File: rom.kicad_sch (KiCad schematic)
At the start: 3 parts, among them U1 74HCT1G08, U2 28C256

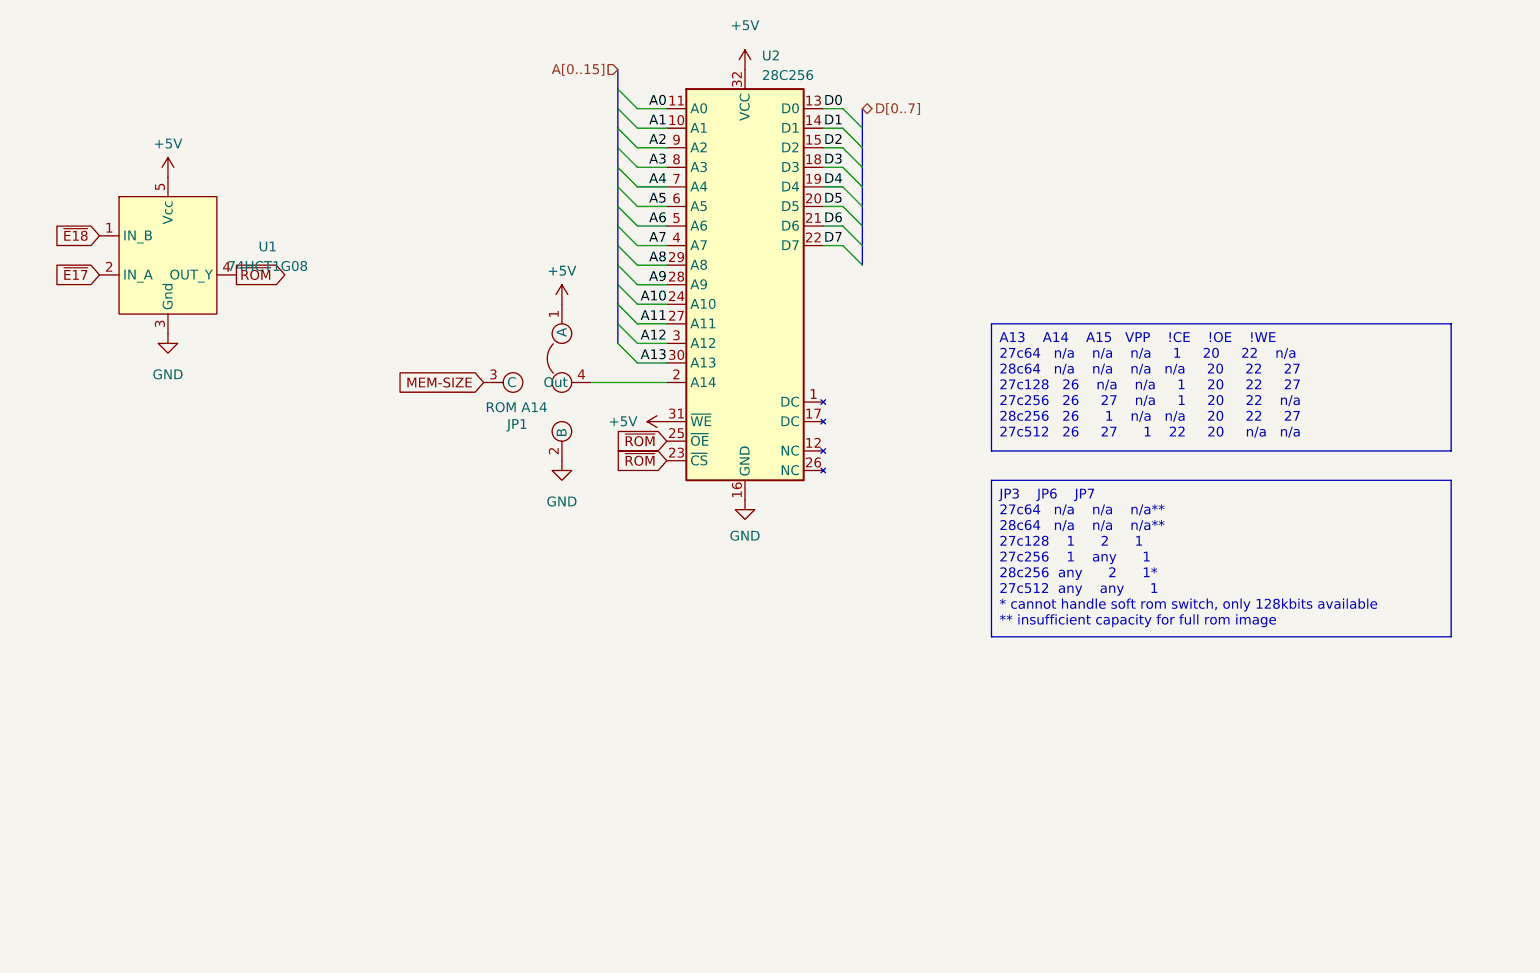
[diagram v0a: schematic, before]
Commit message: migrate to flash rom
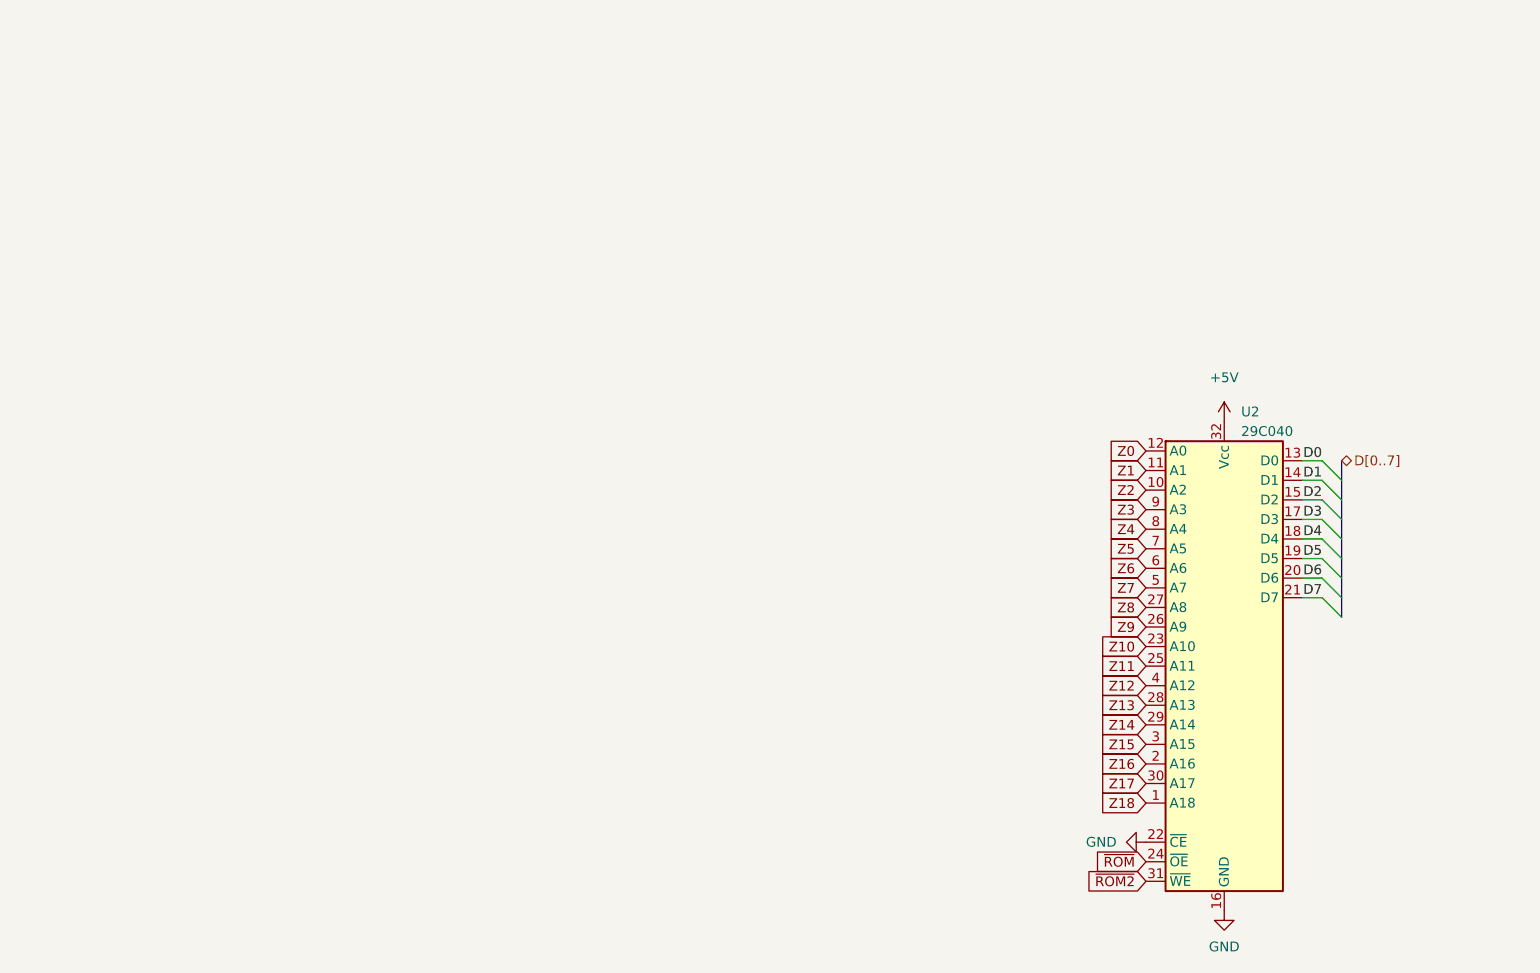
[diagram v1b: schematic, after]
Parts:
- removed JP1: ROM A14, Dragon:Jumper_4, symbol vdg:Jumper_4
- removed U1: 74HCT1G08, Package_TO_SOT_SMD:SOT-353_SC-70-5_Handsoldering, symbol vdg:74HC1G08
- removed U2: 28C256, Package_LCC:PLCC-32_THT-Socket, symbol BenEater:28C256_PLCC
- added U2: 29C040, Package_LCC:PLCC-32_THT-Socket, symbol Motorola PIA:29C040
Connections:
- net +5V: now also U2.32 (Vcc)
- net D0: now also U2.13 (D0)
- net D1: now also U2.14 (D1)
- net D2: now also U2.15 (D2)
- net D3: now also U2.17 (D3)
- net D4: now also U2.18 (D4)
- net D5: now also U2.19 (D5)
- net D6: now also U2.20 (D6)
- net D7: now also U2.21 (D7)
- net GND: now also U2.16 (GND), U2.22 (~{CE})
- net ~{ROM}: now also U2.24 (~{OE})
- new net Z0: U2.12 (A0)
- new net Z1: U2.11 (A1)
- new net Z10: U2.23 (A10)
- new net Z11: U2.25 (A11)
- new net Z12: U2.4 (A12)
- new net Z13: U2.28 (A13)
- new net Z14: U2.29 (A14)
- new net Z15: U2.3 (A15)
- new net Z16: U2.2 (A16)
- new net Z17: U2.30 (A17)
- new net Z18: U2.1 (A18)
- new net Z2: U2.10 (A2)
- new net Z3: U2.9 (A3)
- new net Z4: U2.8 (A4)
- new net Z5: U2.7 (A5)
- new net Z6: U2.6 (A6)
- new net Z7: U2.5 (A7)
- new net Z8: U2.27 (A8)
- new net Z9: U2.26 (A9)
- new net ~{ROM2}: U2.31 (~{WE})
